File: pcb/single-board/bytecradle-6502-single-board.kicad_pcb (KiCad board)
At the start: 2 copper layers, 224.9 x 116.2 mm, 88 parts, among them J1 USB_B, J2 EXPBUS1, J3 EXPBUS2, J4 VIA, J5 UART1, J6 UART2, J7 Serial, J8 Serial, SW1 SW_SPDT, SW2 RESET, SW3 NMI, U1 74HC14, U10 74HC273, U11 74HC273, U12 74HC245, U13 74HC245, U14 74HC10, U15 SST39SF040, U16 AS6C4008, U17 CY62256, U18 74HC688, U19 W65C22NxP, U2 W65C02, U20 74HC688, U21 W65C51NxP, U22 74HC688, U23 W65C51NxP, U3 74HC688, U4 74HC08, U5 74HC688, U6 74HC688, U7 74HC04, U8 74HC10, U9 74HC00, X1 32MHz, Y1 1.8432 MHz, Y2 1.8432 MHz

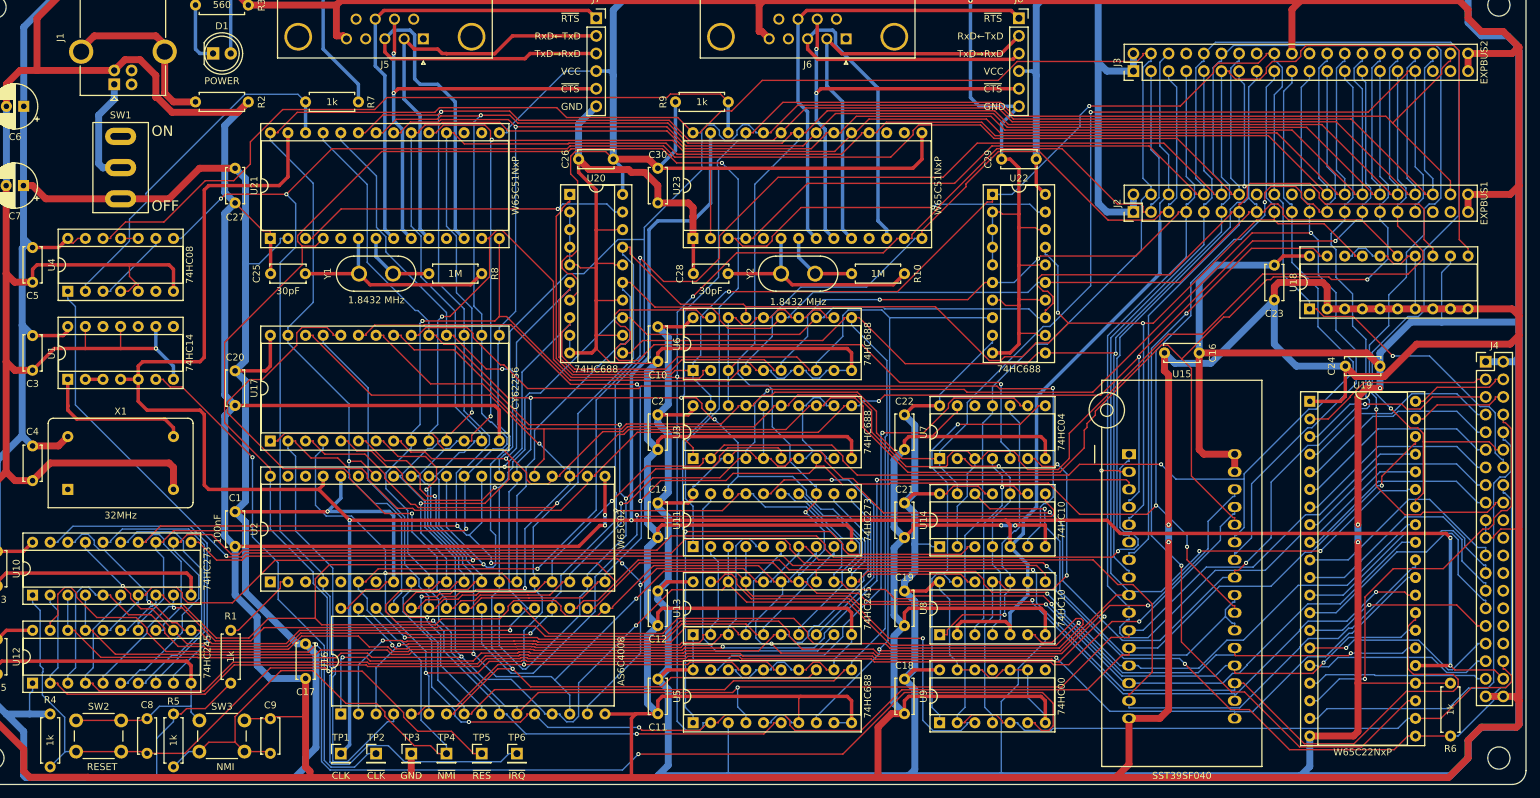
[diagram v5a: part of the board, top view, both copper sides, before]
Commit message: Improving routing
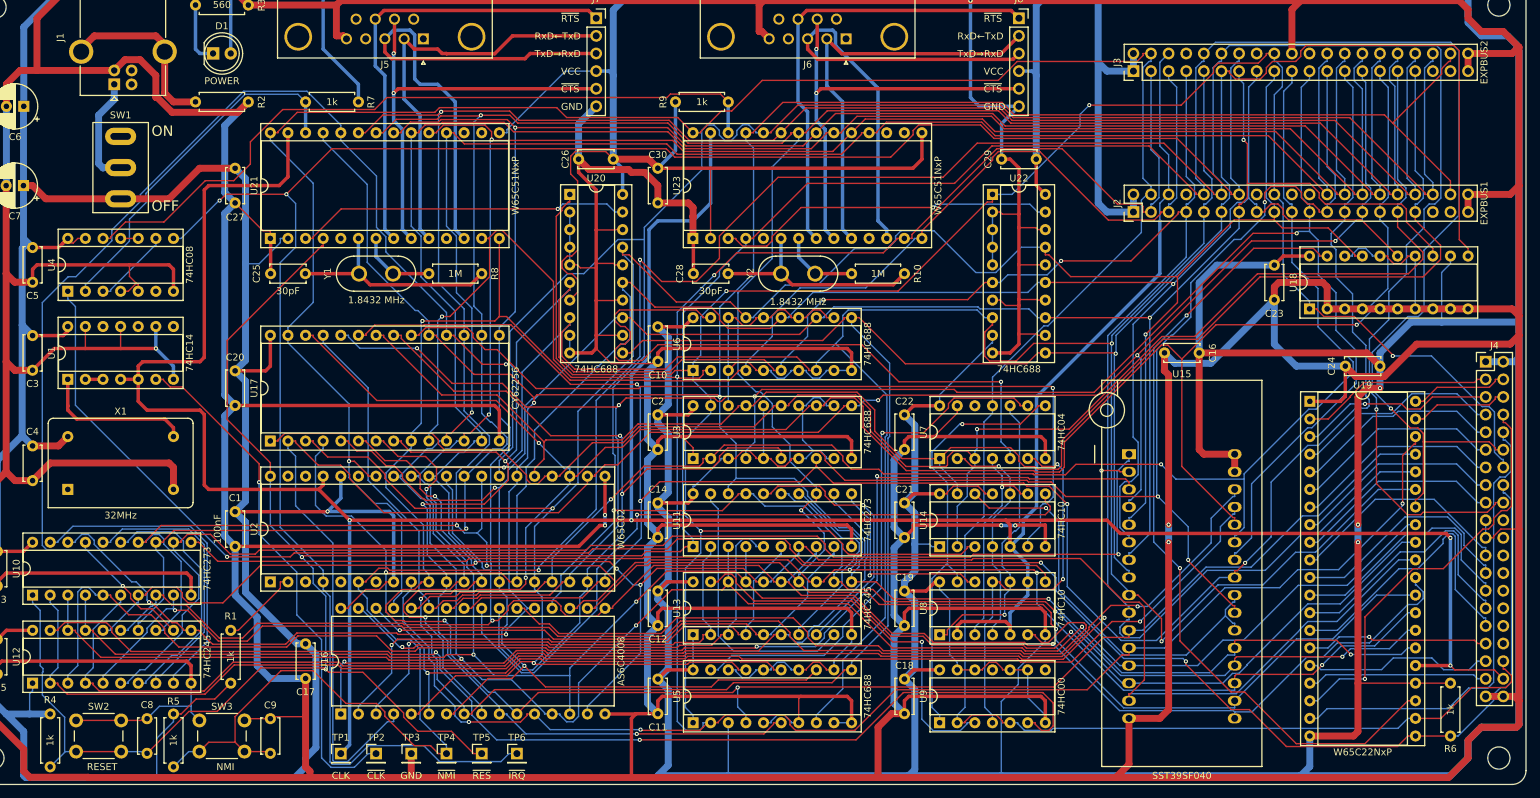
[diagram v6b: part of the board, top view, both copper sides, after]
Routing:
- net D6: track 524.0 -> 565.5 mm, vias 6 -> 5
- net D3: track 523.2 -> 492.8 mm, vias 4 -> 3
- net A5: track 366.0 -> 337.9 mm, vias 3 -> 4
- net ~{RES}: track 526.5 -> 500.8 mm
- net D5: track 539.1 -> 513.6 mm, vias 5 -> 6
- net Net-(U12-CE): track 184.7 -> 166.4 mm
- net A6: track 379.1 -> 363.3 mm, vias 2 -> 3
- net PB4: track 28.1 -> 42.2 mm, vias 1 -> 0
- net A9: track 308.8 -> 295.2 mm
- net A2: track 413.8 -> 400.5 mm, vias 6 -> 5
- net A15: track 239.1 -> 227.4 mm, vias 1 -> 0
- net A1: track 385.3 -> 396.1 mm, vias 2 -> 3
- net A3: track 407.6 -> 400.3 mm, vias 6 -> 5
- net Net-(U10-Q4): track 187.3 -> 183.9 mm
- net A0: track 438.2 -> 441.5 mm
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
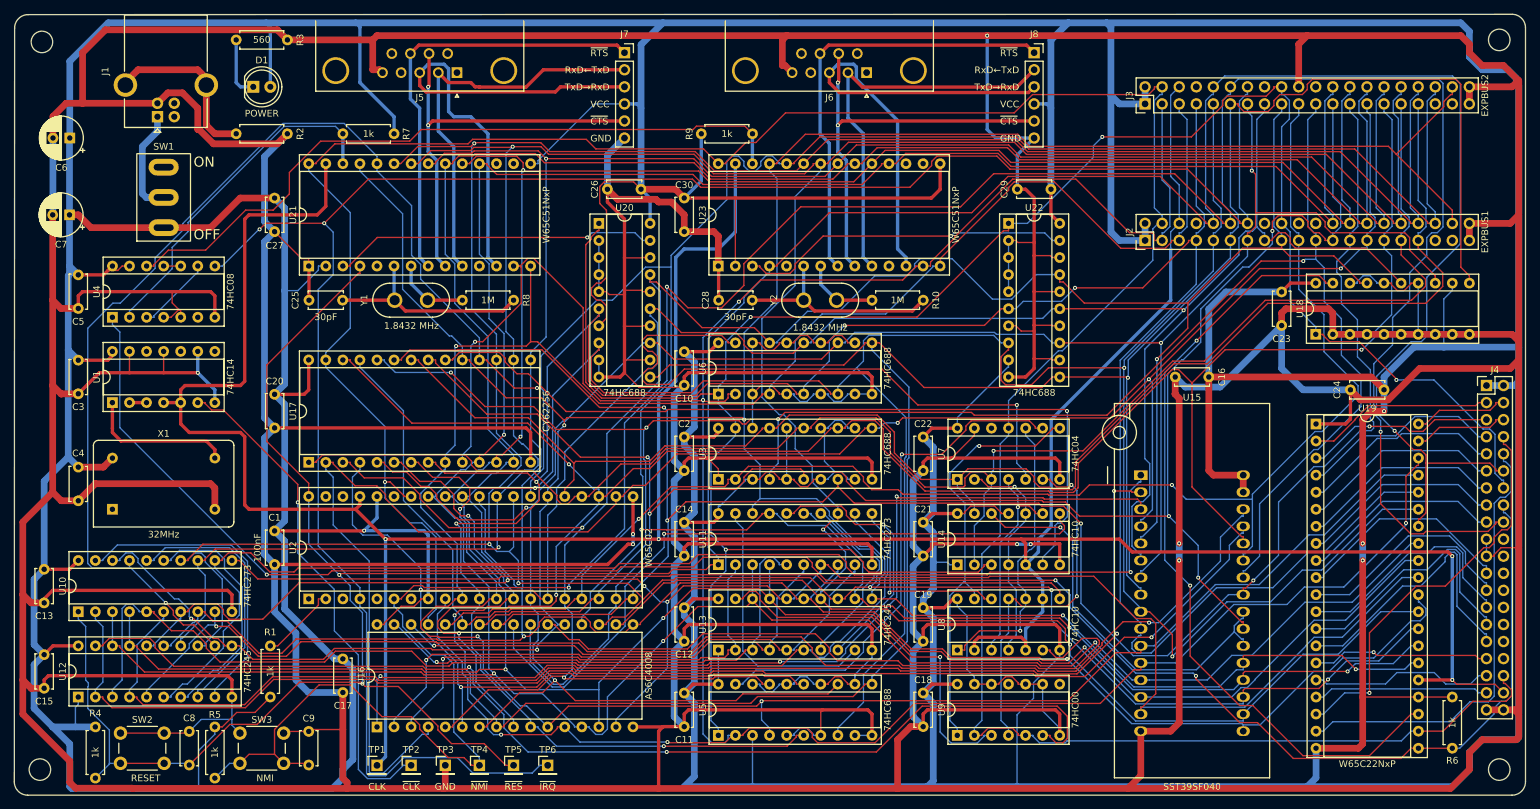
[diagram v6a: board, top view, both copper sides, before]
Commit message: Fixing errors and finalizing SBC design
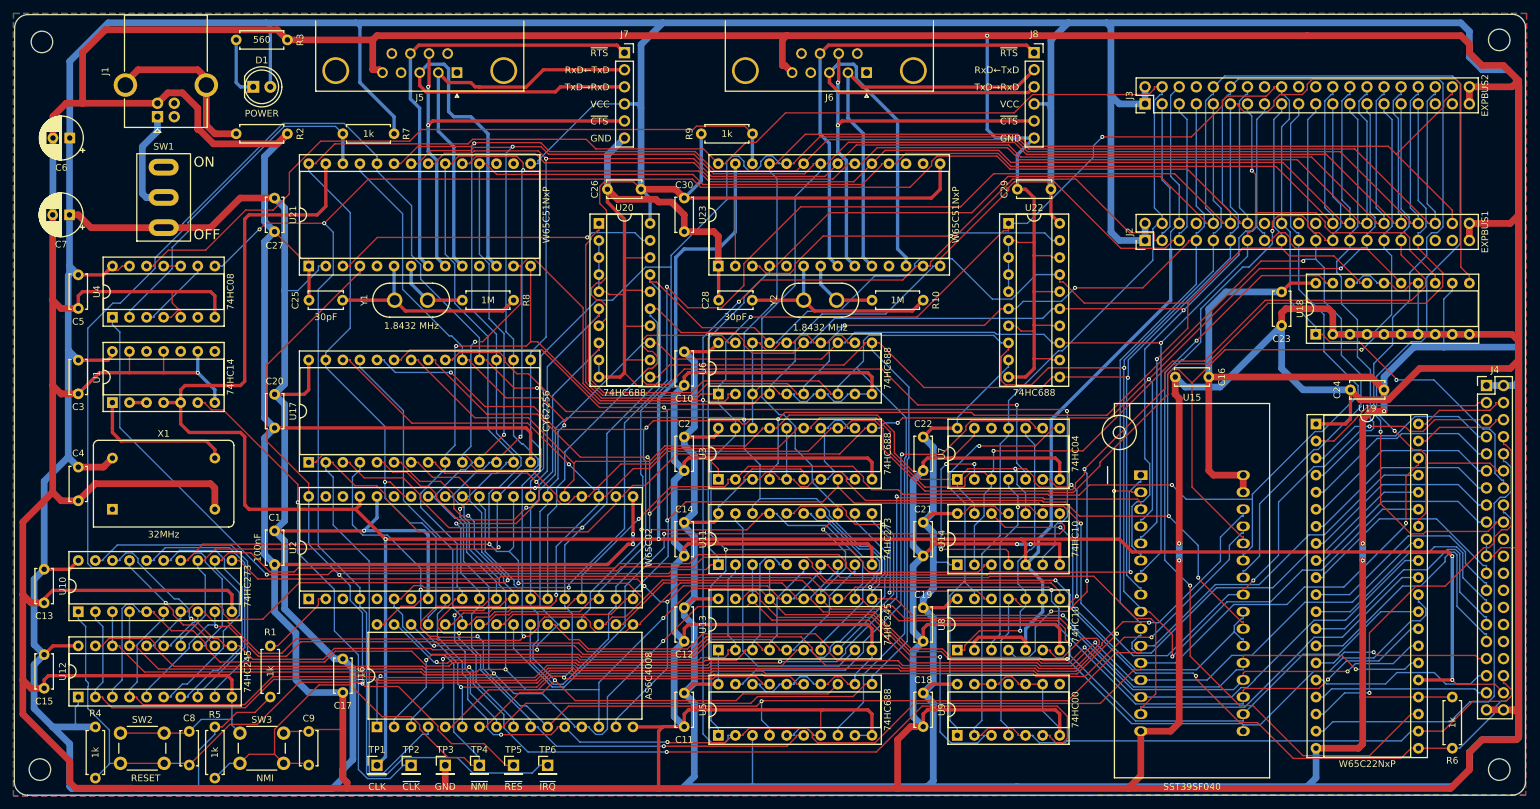
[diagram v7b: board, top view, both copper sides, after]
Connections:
- U14 pad 10: ~{A15} -> A15
- U8 pad 14: GND -> VCC
- U8 pad 4: ~{A15} -> A15
- U8 pad 7: VCC -> GND
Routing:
- net A15: track 227.4 -> 271.3 mm, vias 0 -> 4
- net VCC: track 1618.0 -> 1595.0 mm
- net GND: track 2119.1 -> 2097.2 mm
- net ~{A15}: track 33.5 -> 31.6 mm, vias 1 -> 3
- added copper zone on F.Cu, net GND
- added copper zone on B.Cu, net VCC
